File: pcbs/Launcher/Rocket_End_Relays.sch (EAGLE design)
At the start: 39 parts, among them IC2 LM2576T-ADJ, K4 LD105, K5 LD105, K6 LD105, K7 LD105, T1 BC547, T2 BC547, T3 BC547, T4 BC547, T5 BC547, U1 ARDUINO-MEGAPRO-5V, X1 22-23-2041, X2 22-23-2041, X3 22-23-2021, X7 22-23-2021

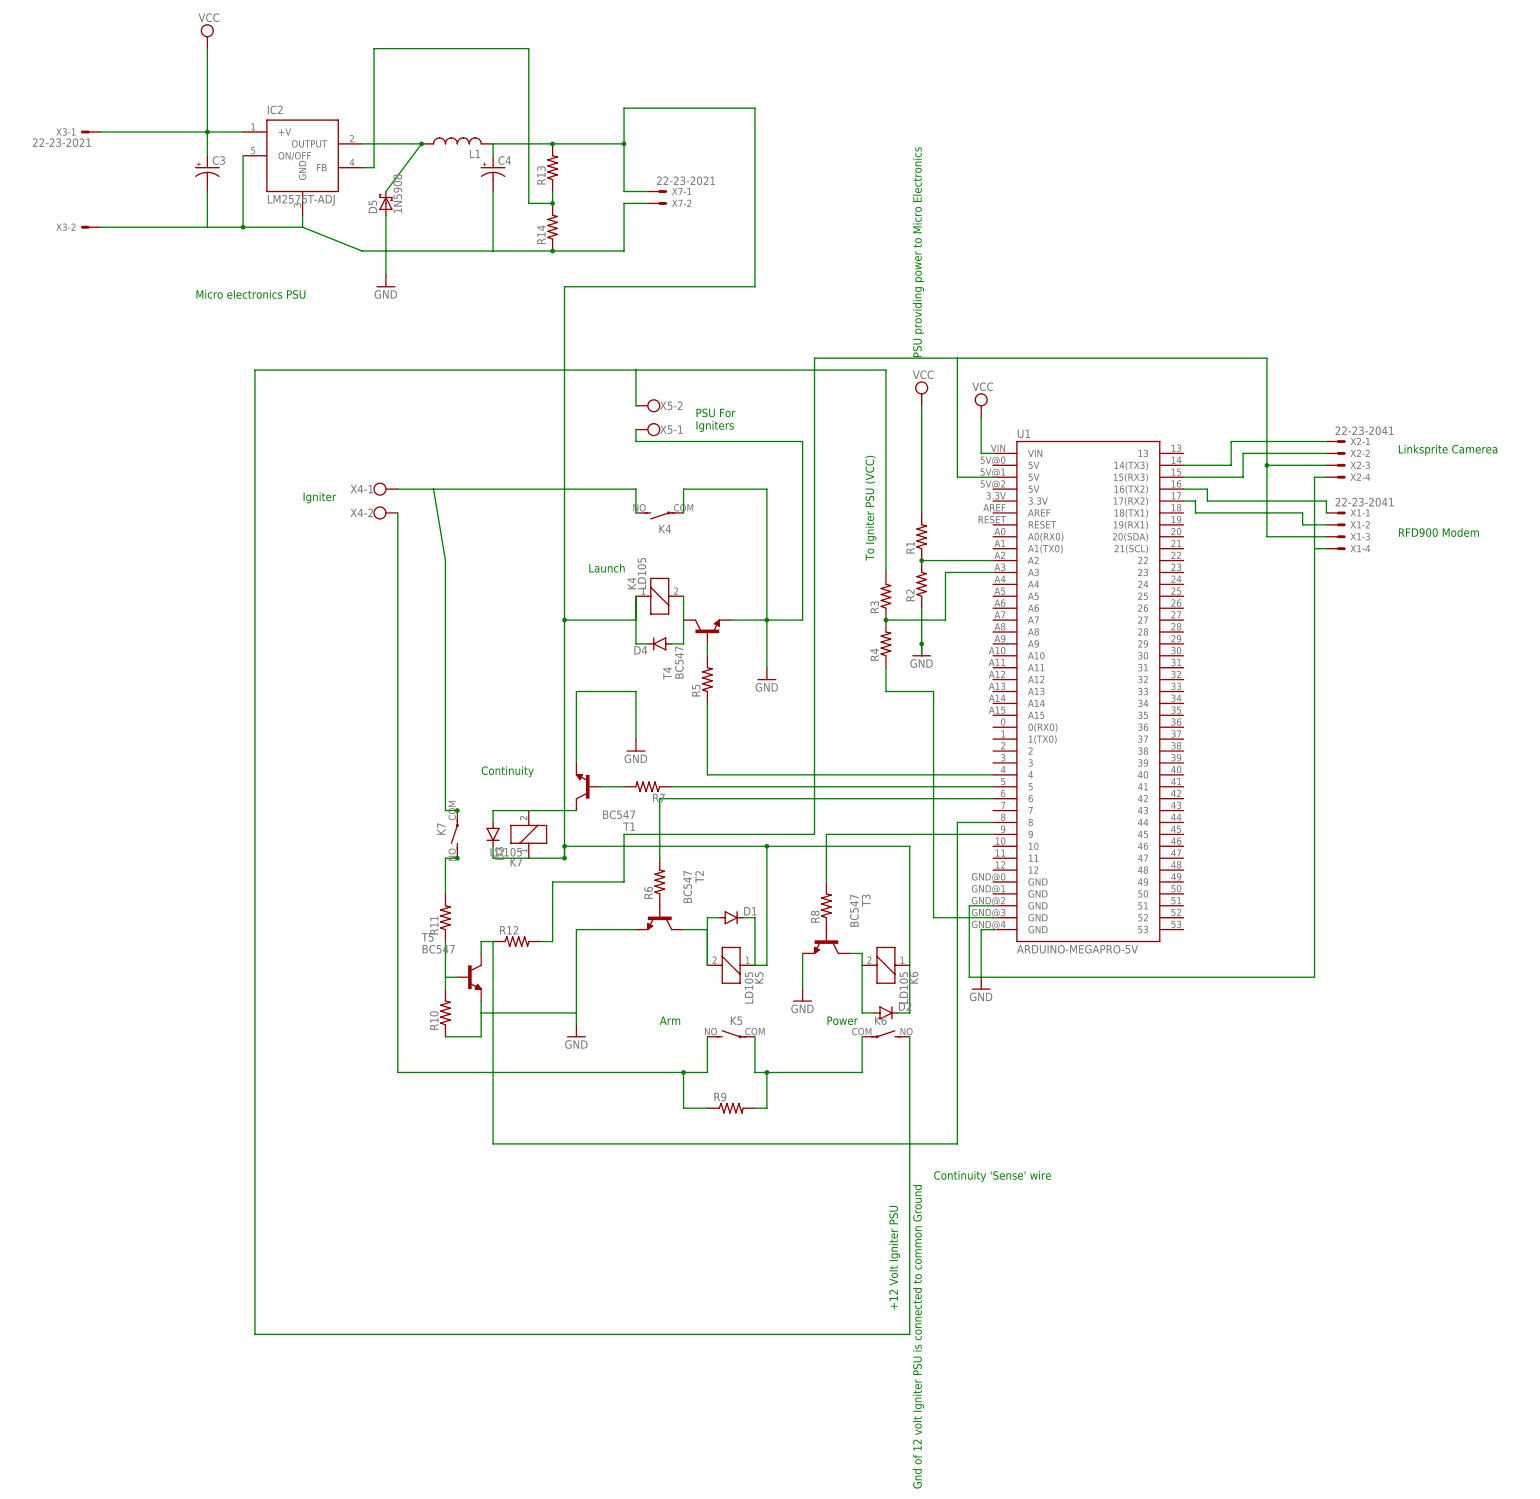
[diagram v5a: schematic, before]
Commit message: * Trying to increase width of particular tracks * Putting in curve tracks to neaten up some areas * Putting in resistor and diode values.
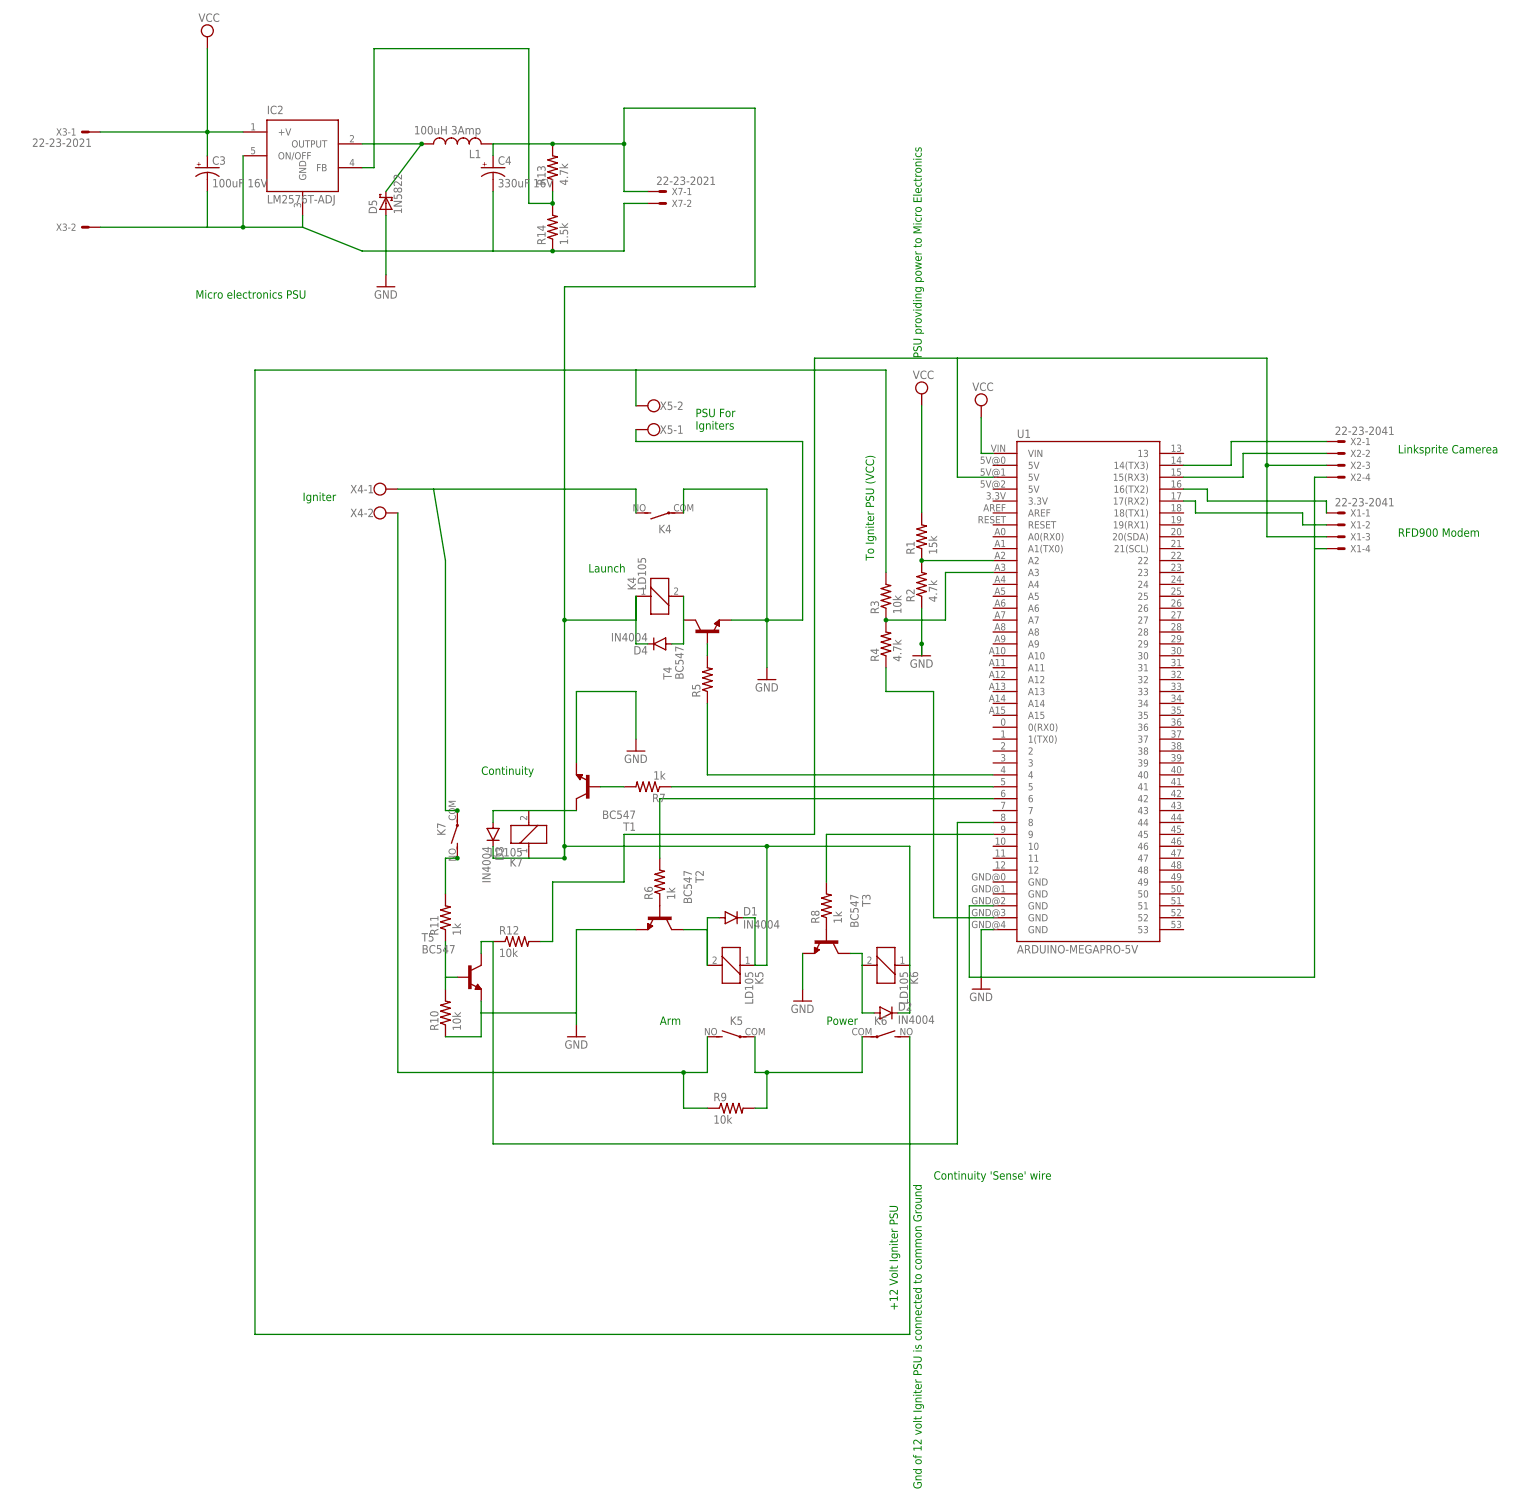
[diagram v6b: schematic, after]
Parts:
- C3: value (none) -> 100uF 16V
- C4: value (none) -> 330uF 16V
- D1, D2, D3, D4: value (none) -> IN4004
- D5: value 1N5908 -> 1N5822
- L1: value (none) -> 100uH 3Amp
- R1: value (none) -> 15k
- R10, R12, R3, R9: value (none) -> 10k
- R11, R6, R7, R8: value (none) -> 1k
- R13, R2, R4: value (none) -> 4.7k
- R14: value (none) -> 1.5k
